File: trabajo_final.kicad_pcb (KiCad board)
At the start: 2 copper layers, 85.7 x 137.2 mm, 26 parts, among them P1 CONN_02X20, P10 CONN_01X20, P11 CONN_01X20, P12 CONN_01X06, P13 CONN_01X06, P14 CONN_02X12, P15 CONN_02X12, P16 CONN_02X12, P17 CONN_02X12, P18 CONN_01X12, P19 CONN_01X12, P2 CONN_01X20, P20 CONN_01X12, P21 CONN_01X12, P3 CONN_02X20, P4 CONN_02X20, P5 CONN_01X19, P6 CONN_02X20, P7 CONN_01X20, P8 CONN_02X20, P9 CONN_02X20

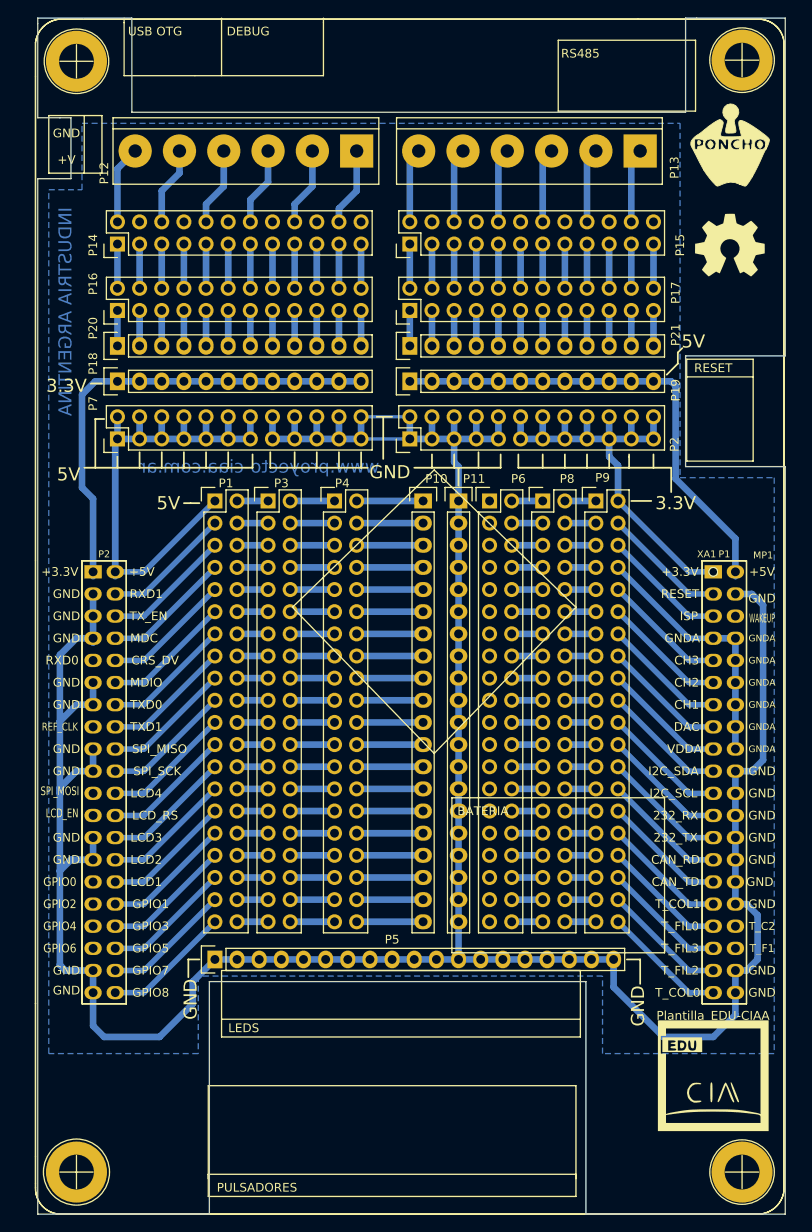
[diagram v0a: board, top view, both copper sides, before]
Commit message: agregada información de cada componente en el esquemático
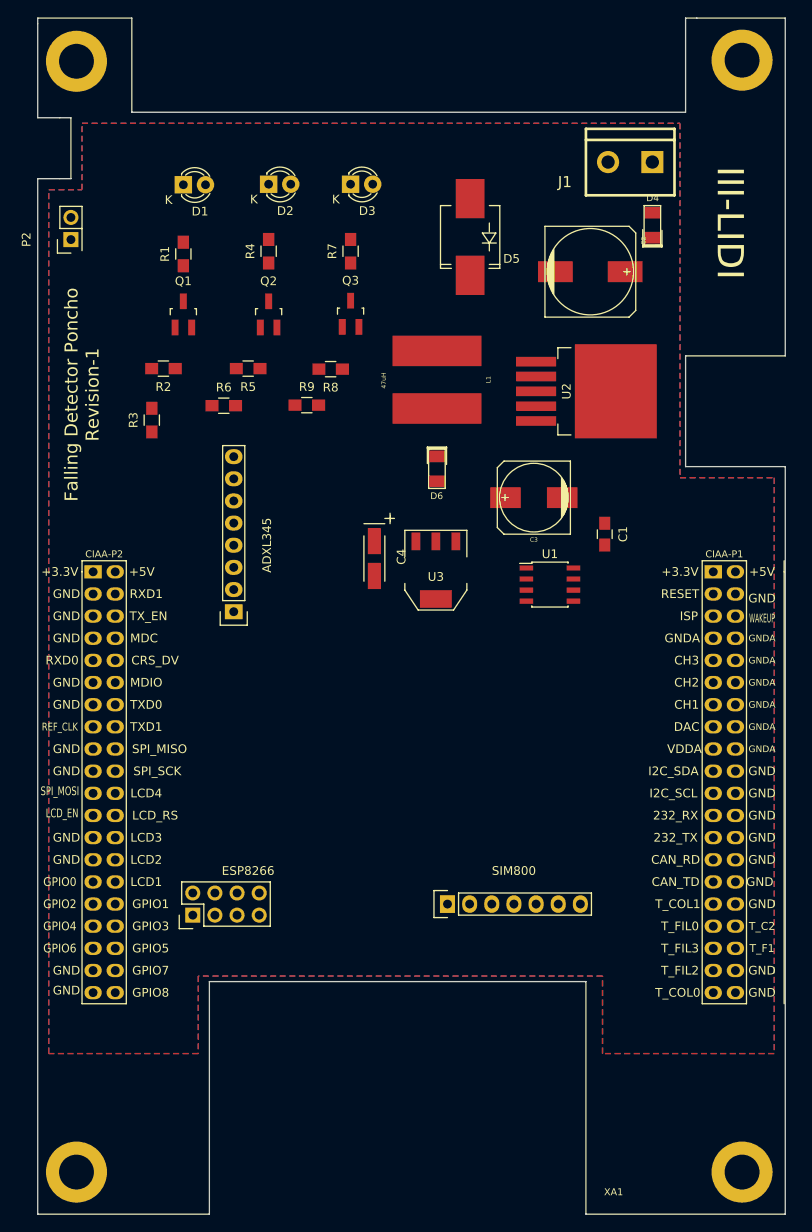
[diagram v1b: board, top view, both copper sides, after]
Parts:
- removed G***: LOGO, Poncho_Esqueleto:Logo_Poncho
- removed G***: Logo_EDU-CIAA, Poncho_Esqueleto:Logo_EDU-CIAA
- removed G101: Logo_OSHWA, Poncho_Esqueleto:Logo_OSHWA
- removed MP1: Plantilla_EDU-CIAA, Poncho_Esqueleto:Plantilla_EDU-CIAA
- removed P1, P3, P4, P6, P8, P9: CONN_02X20, Pin_Headers:Pin_Header_Straight_2x20
- removed P10, P11: CONN_01X20, Pin_Headers:Pin_Header_Straight_1x20
- removed P12, P13: CONN_01X06, mod:bornier6
- removed P14, P15, P16, P17: CONN_02X12, Pin_Headers:Pin_Header_Straight_2x12
- removed P18, P19, P20, P21: CONN_01X12, Pin_Headers:Pin_Header_Straight_1x12
- removed P5: CONN_01X19, Pin_Headers:Pin_Header_Straight_1x19
- removed P7: CONN_01X20, Pin_Headers:Pin_Header_Straight_2x12
- added ADXL345: CONN_01X08, Pin_Headers:Pin_Header_Straight_1x08, F.Cu at (96.1, 93.5)
- added C1: 100nF, Capacitors_SMD:C_0805_HandSoldering, F.Cu at (138.7, 84.6)
- added C2: 470uF, mod:c2, F.Cu at (137.0, 54.5)
- added C3: 330uF, mod:c3, F.Cu at (130.6, 80.4)
- added C4: 10uF, Capacitors_Tantalum_SMD:TantalC_SizeA_EIA-3216_HandSoldering, F.Cu at (112.3, 87.4)
- added D1: LED, LEDs:LED-3MM, F.Cu at (90.4, 44.5)
- added D2: LED, LEDs:LED-3MM, F.Cu at (100.1, 44.5)
- added D3: LED, LEDs:LED-3MM, F.Cu at (109.5, 44.5)
- added D4: PMEG3020EH, mod:SOD123F, F.Cu at (144.1, 49.1)
- added D5: B540C-13-F, mod:SMC_Handsoldering, F.Cu at (123.2, 50.5)
- added D6: SMAZ5V6, mod:SOD123F, F.Cu at (119.4, 77.1)
- added ESP8266: CONN_02X04, Pin_Headers:Pin_Header_Straight_2x04, F.Cu at (91.4, 128.3)
- added J1: TB_1X2, mod:bornier2, F.Cu at (141.6, 41.9)
- added L1: 47uH, mod:SRN1060, F.Cu at (119.4, 66.9)
- added Q1: 2N7002, TO_SOT_Packages_SMD:SOT-23_Handsoldering, F.Cu at (90.4, 59.4)
- added Q2: 2N7002, TO_SOT_Packages_SMD:SOT-23_Handsoldering, F.Cu at (100.1, 59.4)
- added Q3: 2N7002, TO_SOT_Packages_SMD:SOT-23_Handsoldering, F.Cu at (109.5, 59.3)
- added R1: 680, Resistors_SMD:R_0805_HandSoldering, F.Cu at (90.4, 52.5)
- added R2: 10K, Resistors_SMD:R_0805_HandSoldering, F.Cu at (88.1, 65.6)
- added R3: 330K, Resistors_SMD:R_0805_HandSoldering, F.Cu at (86.7, 71.5)
- added R4: 680, Resistors_SMD:R_0805_HandSoldering, F.Cu at (100.1, 52.1)
- added R5: 10K, Resistors_SMD:R_0805_HandSoldering, F.Cu at (97.8, 65.6)
- added R6: 330K, Resistors_SMD:R_0805_HandSoldering, F.Cu at (95.0, 69.8)
- added R7: 680, Resistors_SMD:R_0805_HandSoldering, F.Cu at (109.5, 52.1)
- added R8: 10K, Resistors_SMD:R_0805_HandSoldering, F.Cu at (107.3, 65.7)
- added R9: 330K, Resistors_SMD:R_0805_HandSoldering, F.Cu at (104.5, 69.8)
- added SIM800: CONN_01X07, Pin_Headers:Pin_Header_Straight_1x07, F.Cu at (120.7, 127.0)
- added U1: 24LC64, Housings_SOIC:SOIC-8_3.9x4.9mm_Pitch1.27mm, F.Cu at (132.4, 90.4)
- added U2: LM2596, TO_SOT_Packages_SMD:TO-263-5Lead, F.Cu at (130.8, 68.2)
- added U3: NCP1117ST33T3G, TO_SOT_Packages_SMD:SOT-223, F.Cu at (119.3, 88.7)
- P2: value CONN_01X20 -> CONN_02X01; footprint Pin_Headers:Pin_Header_Straight_2x12 -> Pin_Headers:Pin_Header_Straight_2x01
- XA1: value (none) -> Conn_Poncho2P_2x_20x2; footprint mod:poncho_grande -> mod:Conn_Poncho_Completo
- moved P2 45.1 mm to (77.5, 50.8)
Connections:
- P2 pad 1: GND -> /Circuito Principal/5VReg
- XA1 pad 1: +3.3V -> (no net)
- XA1 pad 11: /Circuito Principal/ADC2 -> (no net)
- XA1 pad 13: /Circuito Principal/ADC1 -> (no net)
- XA1 pad 15: /Circuito Principal/DAC -> (no net)
- XA1 pad 17: +3.3VADC -> (no net)
- XA1 pad 23: /Circuito Principal/RXD -> /Circuito Principal/RS232_RXD
- XA1 pad 25: /Circuito Principal/TXD -> /Circuito Principal/RS232_TXD
- XA1 pad 27: /Circuito Principal/RD -> (no net)
- XA1 pad 29: /Circuito Principal/TD -> (no net)
- XA1 pad 3: /Circuito Principal/RESET -> (no net)
- XA1 pad 31: /Circuito Principal/COL1 -> (no net)
- XA1 pad 33: /Circuito Principal/F0 -> (no net)
- XA1 pad 35: /Circuito Principal/F3 -> (no net)
- XA1 pad 37: /Circuito Principal/F2 -> (no net)
- XA1 pad 39: /Circuito Principal/COL0 -> (no net)
- XA1 pad 41: +3.3VP -> (no net)
- XA1 pad 42: +5VP -> (no net)
- XA1 pad 44: /Circuito Principal/RXD1 -> (no net)
- XA1 pad 46: /Circuito Principal/TXEN -> (no net)
- XA1 pad 48: /Circuito Principal/MDC -> (no net)
- XA1 pad 5: /Circuito Principal/ISP -> (no net)
- XA1 pad 50: /Circuito Principal/CRS -> (no net)
- XA1 pad 52: /Circuito Principal/MDIO -> (no net)
- XA1 pad 54: /Circuito Principal/TXD0 -> (no net)
- XA1 pad 56: /Circuito Principal/TXD1 -> (no net)
- XA1 pad 58: /Circuito Principal/MISO -> (no net)
- XA1 pad 60: /Circuito Principal/spiCCK -> (no net)
- XA1 pad 62: /Circuito Principal/LCD4 -> (no net)
- XA1 pad 64: /Circuito Principal/RS -> (no net)
- XA1 pad 66: /Circuito Principal/LCD3 -> (no net)
- XA1 pad 68: /Circuito Principal/LCD2 -> (no net)
- XA1 pad 70: /Circuito Principal/LCD1 -> (no net)
- XA1 pad 71: (no net) -> /Conector del Poncho/GPIO2
- XA1 pad 72: /Circuito Principal/GPIO1 -> /Conector del Poncho/GPIO1
- XA1 pad 73: (no net) -> /Circuito Principal/GPIO4
- XA1 pad 75: (no net) -> /Circuito Principal/GPIO6
- XA1 pad 78: /Circuito Principal/GPIO7 -> (no net)
- XA1 pad 80: /Circuito Principal/GPIO8 -> (no net)
- XA1 pad 9: /Circuito Principal/ADC3 -> (no net)
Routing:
- net GND: track 336.4 -> 0.00 mm
- net +5VP: track 64.0 -> 0.00 mm
- net +5V: track 55.4 -> 0.00 mm
- net +3.3V: track 54.8 -> 0.00 mm
- net +3.3VP: track 54.0 -> 0.00 mm
- net GNDA: track 29.5 -> 0.00 mm
- net /Circuito Principal/GPIO5: track 14.8 -> 0.00 mm
- net /Circuito Principal/spiCCK: track 14.8 -> 0.00 mm
- net /Circuito Principal/TXEN: track 14.8 -> 0.00 mm
- net /Circuito Principal/TXD1: track 14.8 -> 0.00 mm
- net /Circuito Principal/TXD0: track 14.8 -> 0.00 mm
- net /Circuito Principal/RXD1: track 14.8 -> 0.00 mm
- net /Circuito Principal/RS: track 14.8 -> 0.00 mm
- net /Circuito Principal/MISO: track 14.8 -> 0.00 mm
- net /Circuito Principal/MDIO: track 14.8 -> 0.00 mm
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- added copper zone on F.Cu, net GND
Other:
- board text added: "FALLING DETECTOR"
- board text added: "Falling Detector Poncho Revision-1"
- board text added: "III-LIDI"
- board text removed: "3.3V"
- board text removed: "5V"
- board text removed: "Borrar (Footprint MP1) la Plantilla-EDU-CIAA al finalizar el posicionamiento y definido el borde de PCB."
- board text removed: "Colocar código de Poncho en cobre, serigrafía y rótulo."
- board text removed: "Editar el rótulo"
- board text removed: "Editar el stackup para reflejar cantidad de capas, si se han realizado cálculos de impedancia o si es relevante para el funcionamiento."
- board text removed: "GND"
- board text removed: "INDUSTRIA ARGENTINA"
- board text removed: "PONCHO GRANDE http://www.proyecto-ciaa.com.ar/"
- board text removed: "Para un diseño nuevo luego de modificar el esquemático: 1)Seleccionar el bloque del PCB y cotas. (click-drag-release). 2)Opción de borrar bloque (Botón derecho). 3)Marcar todo menos locked footprints (MP1 y XA1) 4) Aceptar. 5) Volver a cargar el netlist."
- board text removed: "STACK-UP PCB de simple faz Sin requisitos de Stackup"
- board text removed: "www.proyecto-ciaa.com.ar"

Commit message: cambio de pc
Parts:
- moved C1 2.44 mm to (139.1, 87.0)
- moved R3 2.33 mm to (85.1, 69.8), turned to 0 degrees
- moved D6 1.39 mm to (118.1, 77.5), turned to 0 degrees
- moved R6 0.38 mm to (94.6, 69.8)
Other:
- board text added: "Falling Detector Poncho Revision-2"
- board text added: "Matías Dell'Oso"
- board text removed: "Falling Detector Poncho Revision-1"
- board text removed: "III-LIDI"
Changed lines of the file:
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@@
   (general
     (links 92)
-    (no_connects 50)
-    (area 24.275 20.09 283.73971 182.405001)
+    (no_connects 52)
+    (area 24.275 20.09 177.608572 182.405001)
     (thickness 1.6)
     (drawings 32)
@@
   )
   (module Capacitors_SMD:C_0805_HandSoldering (layer F.Cu)
-    (at 138.684 84.582 270)
+    (at 139.065 86.995 270)
     (descr "Capacitor SMD 0805, hand soldering")
     (tags "capacitor 0805")
@@
   )
   (module Resistors_SMD:R_0805_HandSoldering (layer F.Cu)
-    (at 86.741 71.501 90)
+    (at 85.09 69.85)
     (descr "Resistor SMD 0805, hand soldering")
     (tags "resistor 0805")
     (attr smd)
-    (fp_text reference R3 (at 0 -2.1 90) (layer F.SilkS)
-      (effects (font (size 1 1) (thickness 0.15)))
-    )
-    (fp_text value 330K (at 0 2.1 90) (layer F.Fab)
+    (fp_text reference R3 (at 0 -2.1) (layer F.SilkS)
+      (effects (font (size 1 1) (thickness 0.15)))
+    )
+    (fp_text value 330K (at 0 2.1) (layer F.Fab)
       (effects (font (size 1 1) (thickness 0.15)))
     )
@@
     (fp_line (start 0.6 0.875) (end -0.6 0.875) (layer F.SilkS) (width 0.15))
     (fp_line (start -0.6 -0.875) (end 0.6 -0.875) (layer F.SilkS) (width 0.15))
-    (pad 1 smd rect (at -1.35 0 90) (size 1.5 1.3) (layers F.Cu F.Paste F.Mask)
-      (net 2 GND))
-    (pad 2 smd rect (at 1.35 0 90) (size 1.5 1.3) (layers F.Cu F.Paste F.Mask)
+    (pad 1 smd rect (at -1.35 0) (size 1.5 1.3) (layers F.Cu F.Paste F.Mask)
+      (net 2 GND))
+    (pad 2 smd rect (at 1.35 0) (size 1.5 1.3) (layers F.Cu F.Paste F.Mask)
       (net 1 "/Circuito Principal/GPIO3"))
     (model Resistors_SMD.3dshapes/R_0805_HandSoldering.wrl
@@
   )
   (module Resistors_SMD:R_0805_HandSoldering (layer F.Cu)
-    (at 94.996 69.85)
+    (at 94.615 69.85)
     (descr "Resistor SMD 0805, hand soldering")
     (tags "resistor 0805")
@@
   )
   (module mod:SOD123F (layer F.Cu)
-    (at 119.4435 77.089 90)
+    (at 118.11 77.47)
     (descr SOD123F)
     (tags "SMD SODF DEV")
     (autoplace_cost90 10)
     (autoplace_cost180 10)
-    (fp_text reference D6 (at -3.1118 -0.033 180) (layer F.SilkS)
+    (fp_text reference D6 (at -3.1118 -0.033 90) (layer F.SilkS)
       (effects (font (size 0.762 0.762) (thickness 0.12)))
     )
-    (fp_text value SMAZ5V6 (at 0 4.0005 90) (layer F.SilkS) hide
+    (fp_text value SMAZ5V6 (at 0 4.0005) (layer F.SilkS) hide
       (effects (font (size 1.524 1.143) (thickness 0.2032)))
     )
@@
     (fp_line (start 2.25298 -0.9525) (end -2.2479 -0.9525) (layer F.SilkS) (width 0.1524))
     (fp_line (start -2.2479 -0.9525) (end -2.2479 0.94742) (layer F.SilkS) (width 0.1524))
-    (pad 1 smd rect (at -1.42494 0 180) (size 1.80086 1.34112) (layers F.Cu F.Paste F.Mask)
-      (net 2 GND))
-    (pad 2 smd rect (at 1.43002 0 180) (size 1.80086 1.34112) (layers F.Cu F.Paste F.Mask)
+    (pad 1 smd rect (at -1.42494 0 90) (size 1.80086 1.34112) (layers F.Cu F.Paste F.Mask)
+      (net 2 GND))
+    (pad 2 smd rect (at 1.43002 0 90) (size 1.80086 1.34112) (layers F.Cu F.Paste F.Mask)
       (net 24 "/Circuito Principal/5VReg"))
     (model oaa/SOD123F.wrl
@@
     )
   )
-  (gr_text III-LIDI (at 153.035 48.895 270) (layer F.SilkS)
-    (effects (font (size 3 3) (thickness 0.5)))
-  )
-  (gr_text "Falling Detector Poncho\nRevision-1" (at 78.74 68.58 90) (layer F.SilkS)
+  (gr_text "Matías \nDell'Oso" (at 153.67 41.275 -90) (layer F.SilkS)
+    (effects (font (size 3 3) (thickness 0.5)) (justify left))
+  )
+  (gr_text "Falling Detector Poncho\nRevision-2" (at 78.74 68.58 90) (layer F.SilkS)
     (effects (font (size 1.5 1.5) (thickness 0.3)))
   )

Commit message: cambio de pc
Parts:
- added R10: 470, Resistors_SMD:R_0805_HandSoldering, F.Cu at (137.2, 101.6)
- added R11: 270, Resistors_SMD:R_0805_HandSoldering, F.Cu at (127.6, 101.6)
- added U4: Buzzer, mod:Buzzer_12x9.5RM7.6, F.Cu at (109.9, 107.3)
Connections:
- ADXL345 pad 3: (no net) -> Net-(ADXL345-Pad3)
- ADXL345 pad 4: (no net) -> Net-(ADXL345-Pad4)
- ADXL345 pad 5: (no net) -> Net-(ADXL345-Pad5)
- ESP8266 pad 4: (no net) -> Net-(ESP8266-Pad4)
- ESP8266 pad 5: (no net) -> Net-(ESP8266-Pad5)
- ESP8266 pad 6: (no net) -> Net-(ESP8266-Pad6)
- SIM800 pad 1: (no net) -> Net-(SIM800-Pad1)
- SIM800 pad 2: (no net) -> Net-(SIM800-Pad2)
- SIM800 pad 5: (no net) -> Net-(SIM800-Pad5)
- U1 pad 1: (no net) -> Net-(U1-Pad1)
- U1 pad 2: (no net) -> Net-(U1-Pad2)
- U1 pad 3: (no net) -> Net-(U1-Pad3)
- U1 pad 7: (no net) -> Net-(U1-Pad7)
- XA1 pad 1: (no net) -> +3V3
- XA1 pad 10: GNDA -> GND
- XA1 pad 11: (no net) -> /Conector del Poncho/ADC2
- XA1 pad 12: GNDA -> GND
- XA1 pad 13: (no net) -> /Conector del Poncho/ADC1
- XA1 pad 14: GNDA -> GND
- XA1 pad 15: (no net) -> /Conector del Poncho/DAC
- XA1 pad 16: GNDA -> GND
- XA1 pad 17: (no net) -> +3.3VADC
- XA1 pad 18: GNDA -> GND
- XA1 pad 27: (no net) -> /Conector del Poncho/RD
- XA1 pad 29: (no net) -> /Conector del Poncho/TD
- XA1 pad 3: (no net) -> /Conector del Poncho/RESET
- XA1 pad 31: (no net) -> /Conector del Poncho/COL1
- XA1 pad 33: (no net) -> /Conector del Poncho/F0
- XA1 pad 34: (no net) -> /Conector del Poncho/COL2
- XA1 pad 35: (no net) -> /Conector del Poncho/F3
- XA1 pad 36: (no net) -> /Conector del Poncho/F1
- XA1 pad 37: (no net) -> /Conector del Poncho/F2
- XA1 pad 39: (no net) -> /Conector del Poncho/COL0
- XA1 pad 41: (no net) -> +3.3VP
- XA1 pad 42: (no net) -> +5VP
- XA1 pad 44: (no net) -> /Conector del Poncho/RXD1
- XA1 pad 46: (no net) -> /Conector del Poncho/TXEN
- XA1 pad 48: (no net) -> /Conector del Poncho/MDC
- XA1 pad 49: (no net) -> /Conector del Poncho/RXD0
- XA1 pad 5: (no net) -> /Conector del Poncho/ISP
- XA1 pad 50: (no net) -> /Conector del Poncho/CRS
- XA1 pad 52: (no net) -> /Conector del Poncho/MDIO
- XA1 pad 54: (no net) -> /Conector del Poncho/TXD0
- XA1 pad 55: (no net) -> /Conector del Poncho/RCLK
- XA1 pad 56: (no net) -> /Conector del Poncho/TXD1
- XA1 pad 58: (no net) -> /Conector del Poncho/MISO
- XA1 pad 6: (no net) -> /Conector del Poncho/WAKEUP
- XA1 pad 60: (no net) -> /Conector del Poncho/spiSCK
- XA1 pad 61: (no net) -> /Conector del Poncho/MOSI
- XA1 pad 62: (no net) -> /Conector del Poncho/LCD4
- XA1 pad 63: (no net) -> /Conector del Poncho/LCD_EN
- XA1 pad 64: (no net) -> /Conector del Poncho/RS
- XA1 pad 66: (no net) -> /Conector del Poncho/LCD3
- XA1 pad 68: (no net) -> /Conector del Poncho/LCD2
- XA1 pad 69: (no net) -> /Conector del Poncho/GPIO0
- XA1 pad 7: GNDA -> GND
- XA1 pad 70: (no net) -> /Conector del Poncho/LCD1
- XA1 pad 78: (no net) -> /Circuito Principal/GPIO7
- XA1 pad 8: GNDA -> GND
- XA1 pad 80: (no net) -> /Conector del Poncho/GPIO8
- XA1 pad 9: (no net) -> /Circuito Principal/ADC3
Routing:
- net /Circuito Principal/3,3VReg: track 0.00 -> 62.7 mm, vias 0 -> 2
- net /Circuito Principal/5VReg: track 0.00 -> 36.8 mm
- net Net-(D5-Pad2): track 0.00 -> 22.8 mm
- net Net-(C2-Pad1): track 0.00 -> 22.3 mm
- net Net-(D4-Pad1): track 0.00 -> 5.81 mm
- net /Circuito Principal/GPIO4: track 0.00 -> 0.67 mm

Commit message: ruteo casi terminado
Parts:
- added C5: 100nF, Capacitors_SMD:C_0805_HandSoldering, F.Cu at (143.3, 99.1)
- added Q4: 2N7002, TO_SOT_Packages_SMD:SOT-23_Handsoldering, F.Cu at (99.6, 120.4)
- added R12: 10K, Resistors_SMD:R_0805_HandSoldering, F.Cu at (98.0, 115.3)
- added R13: 330K, Resistors_SMD:R_0805_HandSoldering, F.Cu at (93.0, 115.3)
- added R14: 680, Resistors_SMD:R_0805_HandSoldering, F.Cu at (104.6, 118.9)
- R10: value 470 -> 470K
- R11: value 270 -> 270K
- U4: footprint mod:Buzzer_12x9.5RM7.6 -> footprints:Buzzer_12x9.5RM7.6
- moved R11 17.3 mm to (144.8, 103.5), turned to 270 degrees
- moved R10 10.3 mm to (144.8, 94.6), turned to 270 degrees
- moved U4 1.45 mm to (108.7, 108.2), turned to 180 degrees
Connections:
- D1 pad 2: +5V -> /Circuito Principal/5VReg
- D2 pad 2: +5V -> /Circuito Principal/5VReg
- D3 pad 2: +5V -> /Circuito Principal/5VReg
- ESP8266 pad 1: /Circuito Principal/RS232_RXD -> /Conector del Poncho/GPIO2
- ESP8266 pad 8: /Circuito Principal/RS232_TXD -> /Conector del Poncho/GPIO1
- R2 pad 2: /Circuito Principal/GPIO3 -> /Circuito Principal/GPIO4
- R3 pad 2: /Circuito Principal/GPIO3 -> /Circuito Principal/GPIO4
- R5 pad 2: /Circuito Principal/GPIO4 -> /Circuito Principal/GPIO3
- R6 pad 2: /Circuito Principal/GPIO4 -> /Circuito Principal/GPIO3
- SIM800 pad 3: /Conector del Poncho/GPIO1 -> /Circuito Principal/RS232_TXD
- SIM800 pad 4: /Conector del Poncho/GPIO2 -> /Circuito Principal/RS232_RXD
- U4 pad 1: /Circuito Principal/GPIO7 -> /Circuito Principal/5VReg
- U4 pad 2: GND -> Net-(R14-Pad1)
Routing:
- net /Circuito Principal/5VReg: track 36.8 -> 247.2 mm, vias 0 -> 3
- net /Circuito Principal/SCL: track 0.00 -> 83.8 mm, vias 0 -> 2
- net /Circuito Principal/SDA: track 0.00 -> 82.9 mm
- net /Circuito Principal/GPIO5: track 0.04 -> 81.0 mm, vias 0 -> 2
- net /Circuito Principal/GPIO3: track 0.40 -> 73.0 mm
- net /Circuito Principal/GPIO4: track 0.67 -> 72.1 mm
- net Net-(D4-Pad1): track 5.81 -> 58.8 mm, vias 0 -> 2
- net /Circuito Principal/3,3VReg: track 62.7 -> 114.7 mm, vias 2 -> 3
- net /Conector del Poncho/GPIO2: track 0.00 -> 37.7 mm
- net /Circuito Principal/RS232_TXD: track 0.00 -> 37.4 mm
- net /Circuito Principal/GPIO6: track 0.00 -> 35.1 mm
- net /Circuito Principal/RS232_RXD: track 0.00 -> 34.2 mm
- net /Circuito Principal/GPIO7: track 0.00 -> 31.1 mm
- net GND: track 0.00 -> 28.0 mm, vias 0 -> 1
- net /Conector del Poncho/GPIO1: track 0.00 -> 20.4 mm
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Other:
- board text added: "Fall Detector Revision-2"
- board text removed: "Falling Detector Poncho Revision-2"
